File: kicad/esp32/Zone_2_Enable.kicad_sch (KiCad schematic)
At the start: 5 parts, among them SW301 B3F-1150

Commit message: Created rev 1.01 - Addes some more labels and annotations
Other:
- title: (none) -> TL2C-ESP32-1 TL2C Adapter for ESP32
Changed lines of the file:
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@@
 	(generator "eeschema")
 	(generator_version "8.0")
-	(paper "A4")
+	(paper "A3")
+	(title_block
+		(title "TL2C-ESP32-1 TL2C Adapter for ESP32")
+		(date "2024-02-08")
+		(rev "1.01")
+	)
 	(junction
 		(at 107.95 62.23)

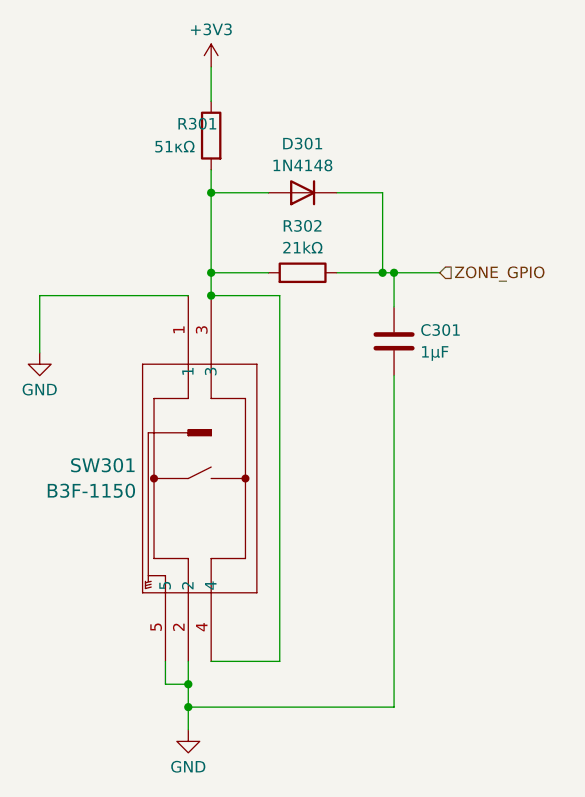
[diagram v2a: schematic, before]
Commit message: Reseated the RJ45
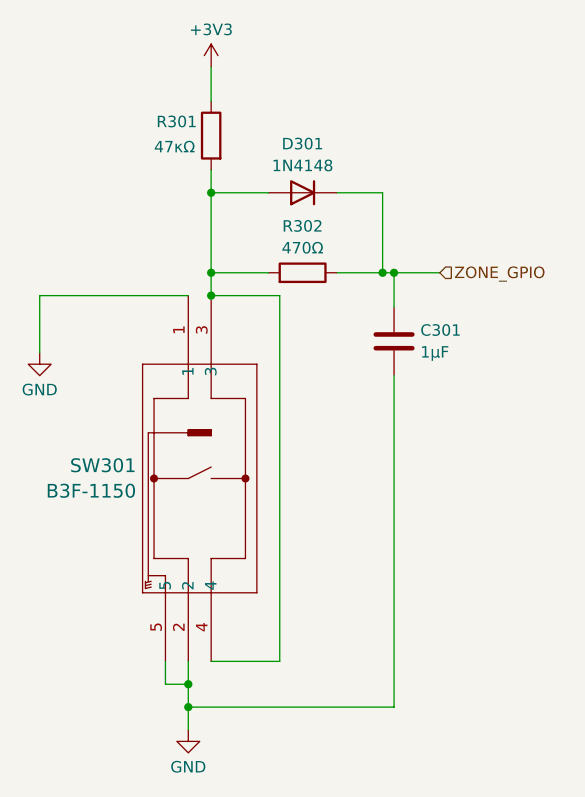
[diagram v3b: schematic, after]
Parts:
- R301: value 51κΩ -> 47κΩ
- R302: value 21kΩ -> 470Ω
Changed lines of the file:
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@@
 			)
 		)
-		(property "Value" "21kΩ"
+		(property "Value" "470Ω"
 			(at 99.06 59.4939 90)
 			(effects
@@
 		(dnp no)
 		(property "Reference" "R301"
-			(at 85.09 45.72 0)
+			(at 82.804 45.466 0)
 			(effects
 				(font
@@
 			)
 		)
-		(property "Value" "51κΩ"
+		(property "Value" "47κΩ"
 			(at 82.55 48.26 0)
 			(effects

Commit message: R1 correction
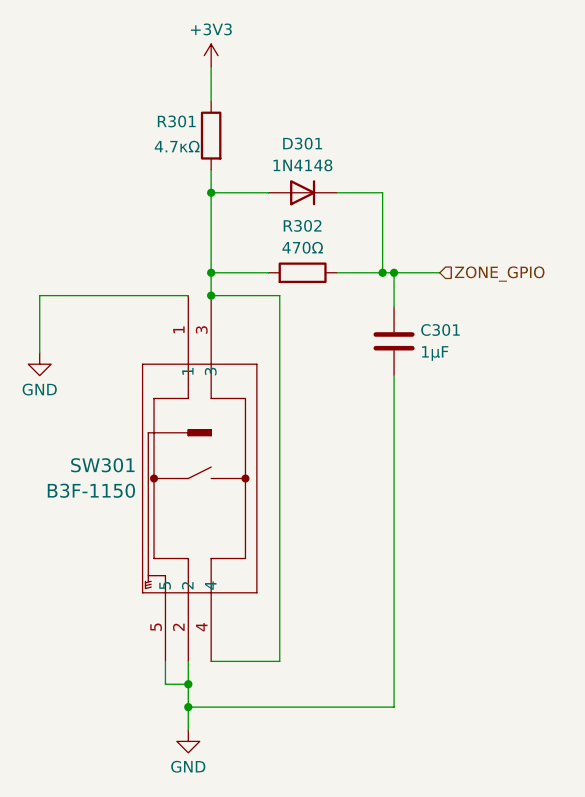
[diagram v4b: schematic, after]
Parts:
- R301: value 47κΩ -> 4.7κΩ
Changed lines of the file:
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@@
 			)
 		)
-		(property "Value" "47κΩ"
+		(property "Value" "4.7κΩ"
 			(at 82.55 48.26 0)
 			(effects

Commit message: Adding some documentation
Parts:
- C301: value 1μF -> 0.1μF
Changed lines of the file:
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@@
 			)
 		)
-		(property "Value" "1μF"
+		(property "Value" "0.1μF"
 			(at 112.141 71.0621 0)
 			(effects

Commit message: Updated the artwork and documentation
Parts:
- R301: value 4.7κΩ -> 10κΩ
- R302: value 470Ω -> 10κΩ
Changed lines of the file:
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@@
 		(fields_autoplaced yes)
 		(property "Reference" "R302"
-			(at 99.06 57.0697 90)
-			(effects
-				(font
-					(size 1.27 1.27)
-				)
-			)
-		)
-		(property "Value" "470Ω"
-			(at 99.06 59.4939 90)
+			(at 99.06 57.0695 90)
+			(effects
+				(font
+					(size 1.27 1.27)
+				)
+			)
+		)
+		(property "Value" "10κΩ"
+			(at 99.06 59.4938 90)
 			(effects
 				(font
@@
 			)
 		)
-		(property "Value" "4.7κΩ"
+		(property "Value" "10κΩ"
 			(at 82.55 48.26 0)
 			(effects
